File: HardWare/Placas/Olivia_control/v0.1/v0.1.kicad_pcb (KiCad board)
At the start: 2 copper layers, 100 x 100 mm, 47 parts, among them J1 PROG, J10 Motor_B, J11 I2C, J12 DAC, J13 UART2, J15 TRIAC_220VAC, J17 In12V, J2 Input1, J3 Input2, J4 Input3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

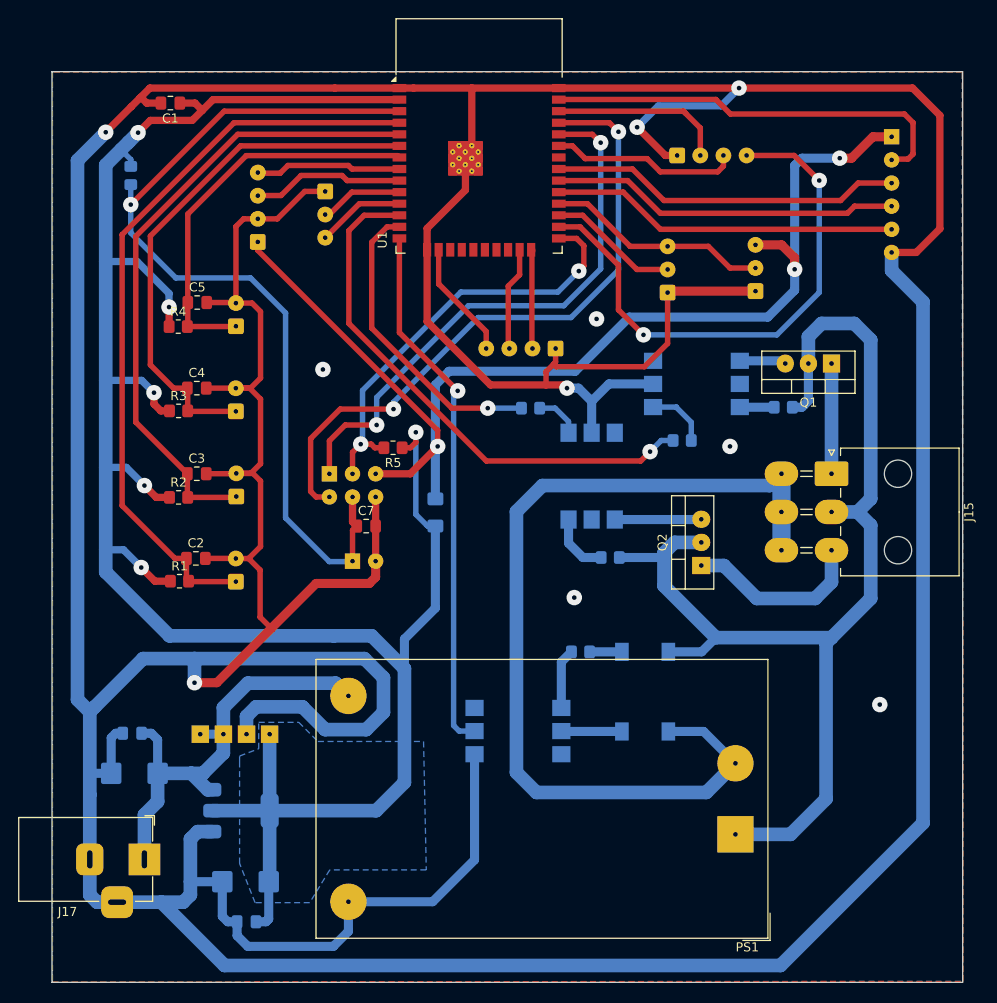
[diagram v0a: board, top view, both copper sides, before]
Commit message: various fix. Traces:0,5. Clearance:1,0
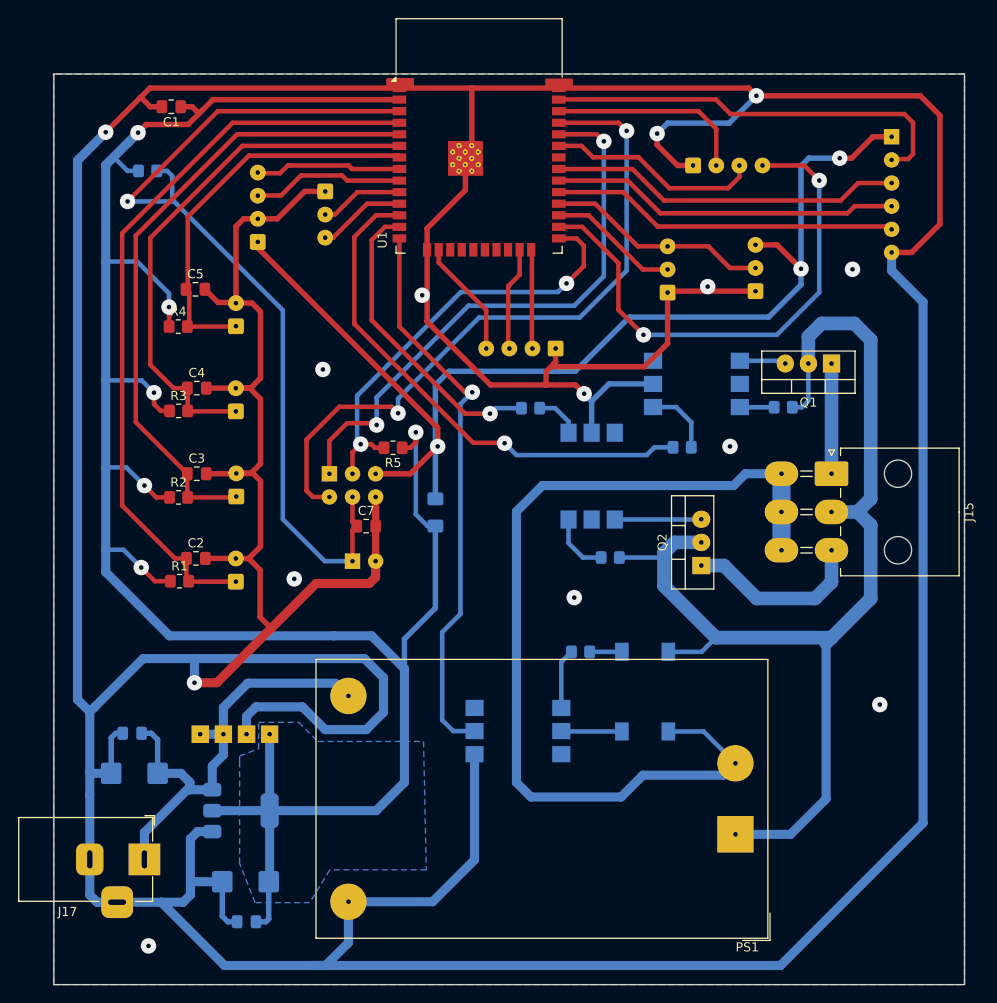
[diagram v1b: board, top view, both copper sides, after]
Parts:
- moved J10 2.07 mm to (170.2, 55.0)
- moved R6 1.92 mm to (110.3, 55.6), turned to 0 degrees
- moved C5 1.46 mm to (115.5, 68.7)
- moved R8 0.75 mm to (169.0, 86.0)
- moved C1 0.41 mm to (112.9, 48.6)
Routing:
- net GND: track 733.1 -> 722.2 mm, vias 10 -> 14
- net /TXD0: track 72.2 -> 76.6 mm
- net /ZERO: track 58.9 -> 62.1 mm
- net /IN_B_P: track 20.7 -> 23.5 mm
- net /TRIAC_A: track 59.1 -> 56.7 mm
- net /IN_B_N: track 19.7 -> 22.1 mm
- net /EN_B: track 59.7 -> 57.7 mm
- net /EN: track 99.6 -> 101.3 mm
- net /RXD0: track 61.8 -> 63.3 mm
- net /NEUTRO: track 103.0 -> 104.0 mm
- net +3.3V: track 248.6 -> 249.5 mm
- net Net-(R8-Pad2): track 6.92 -> 7.67 mm
